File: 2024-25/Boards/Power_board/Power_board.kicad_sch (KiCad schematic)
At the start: 17 parts, among them J1 430451001

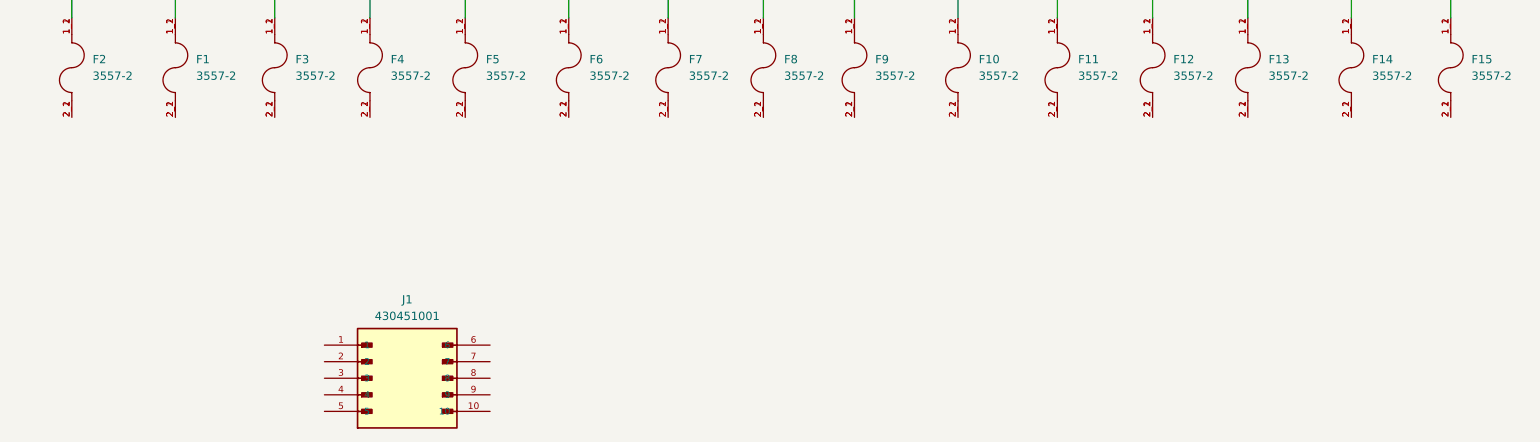
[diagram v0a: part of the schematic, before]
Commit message: added busbar board
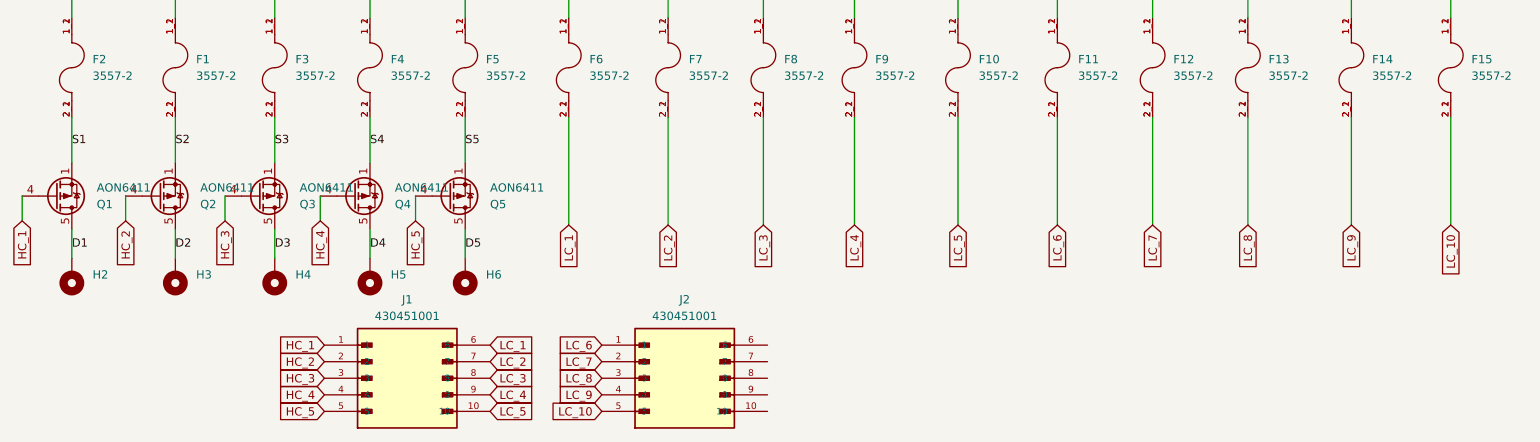
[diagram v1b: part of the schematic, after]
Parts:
- added H2, H3, H4, H5, H6: MountingHole_Pad, MountingHole:MountingHole_5.3mm_M5_Pad, symbol Mechanical:MountingHole_Pad
- added J2: 430451001, 0430451001:MOLEX_430451001, symbol 0430451001:430451001
- added Q1, Q2, Q3, Q4, Q5: AON6411, Package_DFN_QFN:AO_DFN-8-1EP_5.55x5.2mm_P1.27mm_EP4.12x4.6mm, symbol Transistor_FET:AON6411
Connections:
- net S4: now reaches F4.2_1, F4.2_2
- net S4: now also Q4.1 (S), Q4.2 (S), Q4.3 (S)
- net S5: now reaches F5.2_1, F5.2_2
- net S5: now also Q5.1 (S), Q5.2 (S), Q5.3 (S)
- net LC_3: now reaches F8.2_1, F8.2_2
- net LC_3: now also J1.8
- net S3: now reaches F3.2_1, F3.2_2
- net S3: now also Q3.1 (S), Q3.2 (S), Q3.3 (S)
- net LC_7: now reaches F12.2_1, F12.2_2
- net LC_7: now also J2.2
- net S1: now reaches F2.2_1, F2.2_2
- net S1: now also Q1.1 (S), Q1.2 (S), Q1.3 (S)
- net S2: now reaches F1.2_1, F1.2_2
- net S2: now also Q2.1 (S), Q2.2 (S), Q2.3 (S)
- net HC_1: now reaches J1.1
- net HC_1: now also Q1.4 (G)
- net LC_5: now reaches J1.10
- net LC_5: now also F10.2_1, F10.2_2
- net HC_2: now reaches J1.2
- net HC_2: now also Q2.4 (G)
- net HC_3: now reaches J1.3
- net HC_3: now also Q3.4 (G)
- net HC_4: now reaches J1.4
- net HC_4: now also Q4.4 (G)
- net HC_5: now reaches J1.5
- net HC_5: now also Q5.4 (G)
- net LC_1: now reaches J1.6
- net LC_1: now also F6.2_1, F6.2_2
- net LC_2: now reaches J1.7
- net LC_2: now also F7.2_1, F7.2_2
- net LC_4: now reaches J1.9
- net LC_4: now also F9.2_1, F9.2_2
- net LC_8: now reaches F13.2_1, F13.2_2
- net LC_8: now also J2.3
- net LC_9: now reaches F14.2_1, F14.2_2
- net LC_9: now also J2.4
- net LC_6: now reaches F11.2_1, F11.2_2
- net LC_6: now also J2.1
- net LC_10: now reaches F15.2_1, F15.2_2
- net LC_10: now also J2.5
- new net D1: H2.1, Q1.5 (D)
- new net D2: H3.1, Q2.5 (D)
- new net D3: H4.1, Q3.5 (D)
- new net D4: H5.1, Q4.5 (D)
- new net D5: H6.1, Q5.5 (D)

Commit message: organizational changes
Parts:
- added H7: MountingHole_Pad, MountingHole:MountingHole_5.3mm_M5_Pad, symbol Mechanical:MountingHole_Pad
- added Q10, Q6, Q7, Q8, Q9: AO3400, Package_TO_SOT_SMD:SOT-23-3, symbol Simulation_SPICE:NMOS
- added R1, R2, R3, R4, R5: 10k, symbol Device:R_Small_US
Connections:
- net HC_1: now also Q6.2 (G); no longer Q1.4 (G)
- net HC_2: now also Q7.2 (G); no longer Q2.4 (G)
- net HC_3: now also Q8.2 (G); no longer Q3.4 (G)
- net HC_4: now also Q9.2 (G); no longer Q4.4 (G)
- net HC_5: now also Q10.2 (G); no longer Q5.4 (G)
- net 12V+: now reaches F1.1_1, F1.1_2, F10.1_1, F10.1_2, F11.1_1, F11.1_2, F12.1_1, F12.1_2, F13.1_1, F13.1_2, F14.1_1, F14.1_2, F15.1_1, F15.1_2, F2.1_1, F2.1_2, F3.1_1, F3.1_2, F4.1_1, F4.1_2, F5.1_1, F5.1_2, F6.1_1, F6.1_2, F7.1_1, F7.1_2, F8.1_1, F8.1_2, F9.1_1, F9.1_2, H1.1
- net 12V+: now also R1.1, R2.1, R3.1, R4.1, R5.1
- net GND: now reaches J2.10
- net GND: now also J2.6, J2.7, J2.8, J2.9, H7.1, Q10.3 (S), Q6.3 (S), Q7.3 (S), Q8.3 (S), Q9.3 (S)
- new net: Q4.4 (G), Q9.1 (D), R4.2
- new net: Q1.4 (G), Q6.1 (D), R1.2
- new net: Q2.4 (G), Q7.1 (D), R2.2
- new net: Q10.1 (D), Q5.4 (G), R5.2
- new net: Q3.4 (G), Q8.1 (D), R3.2
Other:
- note added: "Battery negative terminal"
- note added: "Battery positive terminal"
- moved on the sheet: F1, F10, F11, F12, F13, F14, F15, F2, F3, F4, F5, F6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

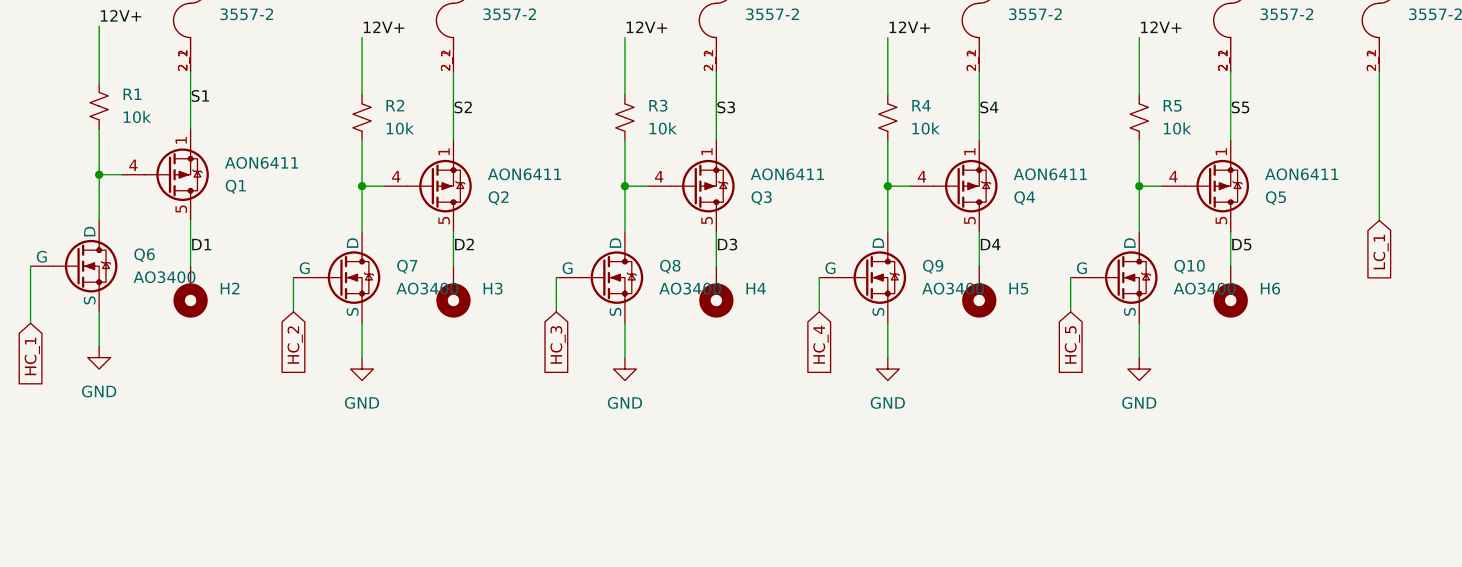
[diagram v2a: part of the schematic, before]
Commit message: accum and HV box schm
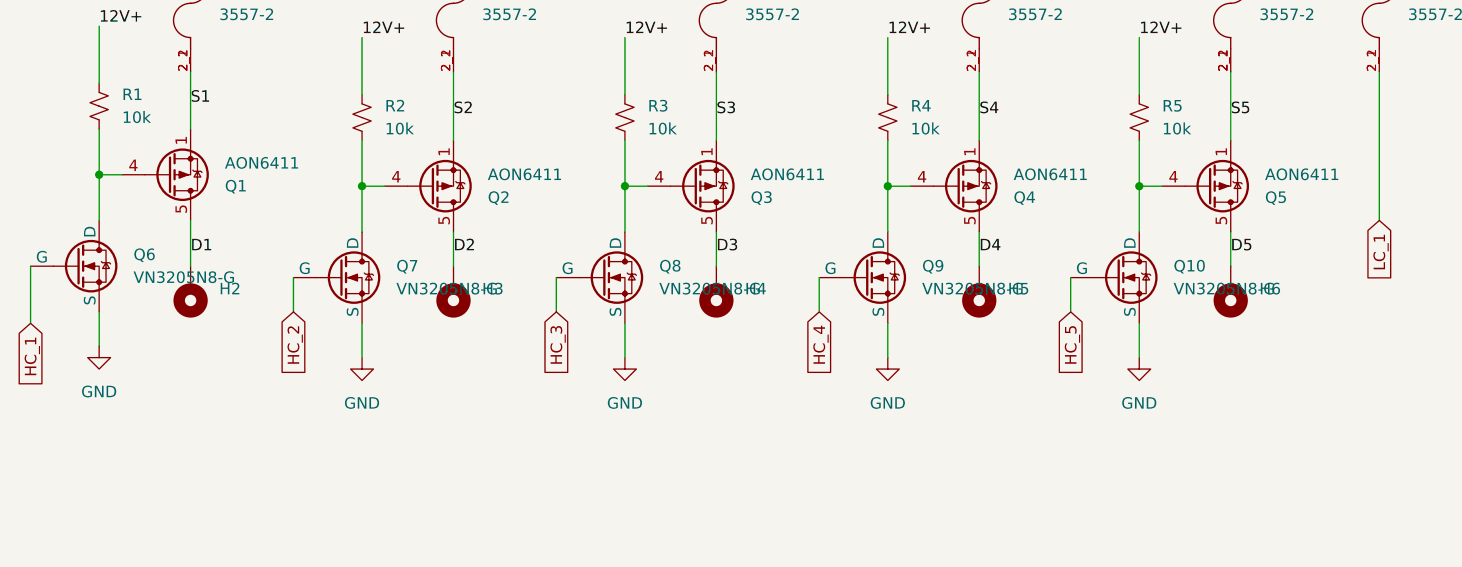
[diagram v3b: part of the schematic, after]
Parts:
- Q10, Q6, Q7, Q8, Q9: value AO3400 -> VN3205N8-G; footprint Package_TO_SOT_SMD:SOT-23-3 -> VN3205N8-G:AMP_PHA-1_
- R1, R2, R3, R4, R5: footprint (none) -> Resistor_SMD:R_0805_2012Metric_Pad1.20x1.40mm_HandSolder

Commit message: full schem
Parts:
- added J3: Conn_01x06_Socket, symbol Connector:Conn_01x06_Socket
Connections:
- net D1 is gone; now on net HC_1: H2.1, Q1.5 (D)
- net D2 is gone; now on net HC_2: H3.1, Q2.5 (D)
- net D3 is gone; now on net HC_3: H4.1, Q3.5 (D)
- net D4 is gone; now on net HC_4: H5.1, Q4.5 (D)
- net D5 is gone; now on net HC_5: H6.1, Q5.5 (D)
- net HC_1: no longer Q6.2 (G)
- net HC_2: no longer Q7.2 (G)
- net HC_3: no longer Q8.2 (G)
- net HC_4: no longer Q9.2 (G)
- net HC_5: no longer Q10.2 (G)
- new net HC_1_pwm: J3.1 (Pin_1), Q6.2 (G)
- new net HC_2_pwm: J3.2 (Pin_2), Q7.2 (G)
- new net HC_3_pwm: J3.3 (Pin_3), Q8.2 (G)
- new net HC_4_pwm: J3.4 (Pin_4), Q9.2 (G)
- new net HC_5_pwm: J3.5 (Pin_5), Q10.2 (G)

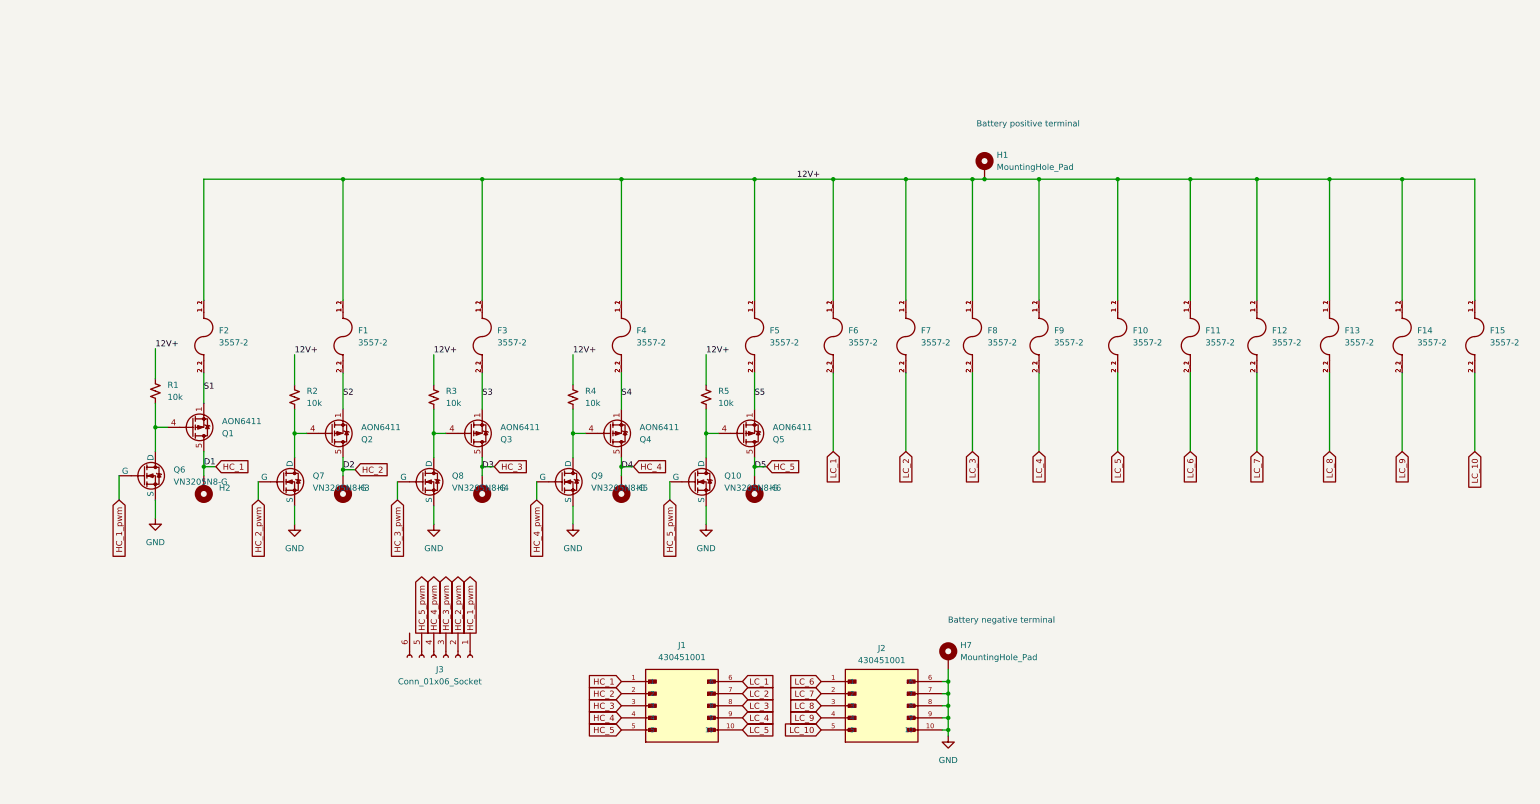
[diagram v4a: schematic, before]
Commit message: Removed extra fuses/high current switches/extra connectors
Removed said items, updated footprints, PCB, and symbols for power board
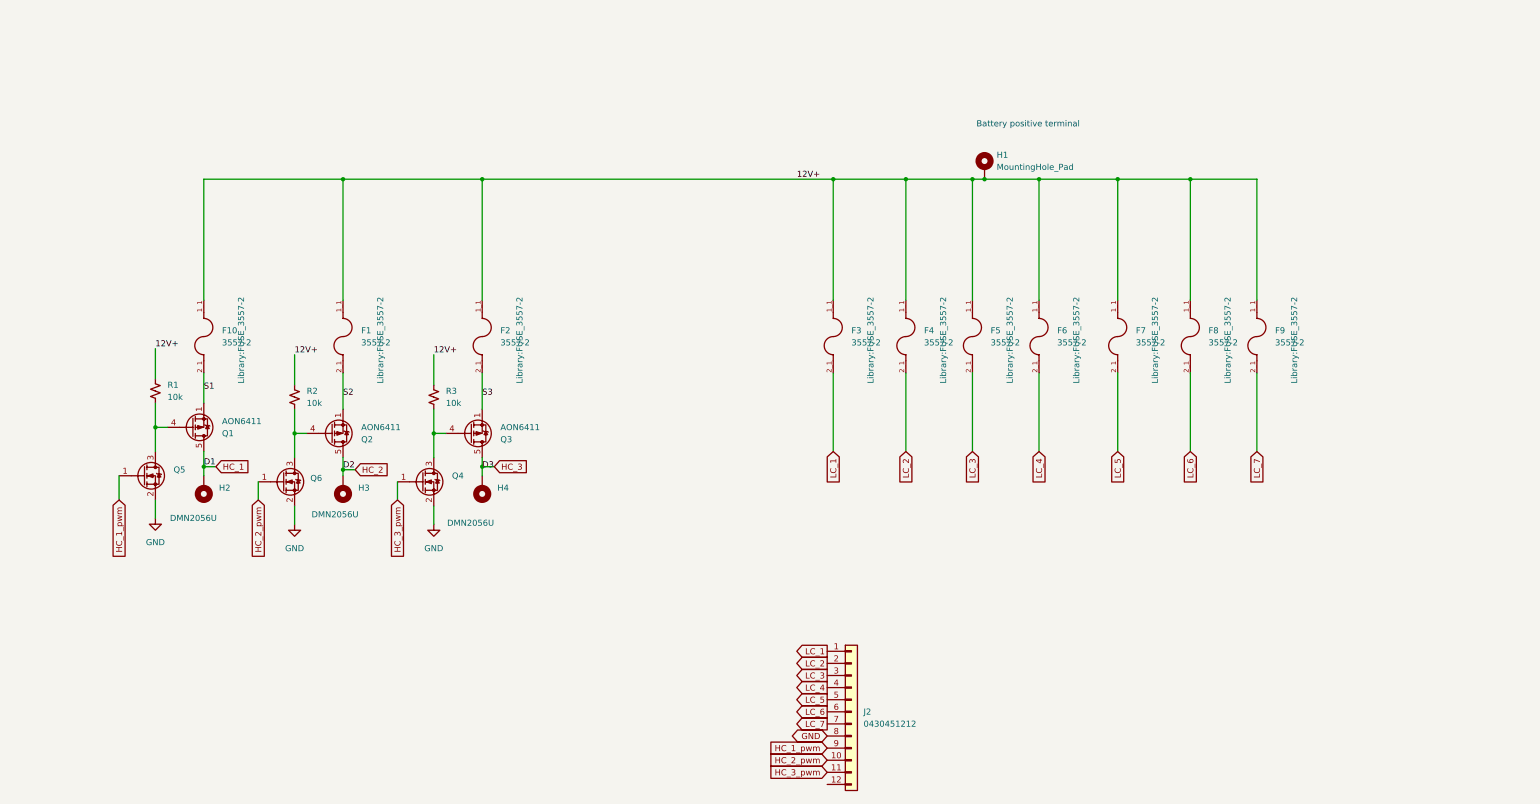
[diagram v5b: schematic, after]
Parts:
- removed F1, F10, F11, F12, F13, F14, F15, F2, F3, F4, F5, F6, F7, F8, F9: 3557-2, 3557-2:FUSE_3557-2, symbol 3557-2:3557-2
- removed H5, H6, H7: MountingHole_Pad, MountingHole:MountingHole_5.3mm_M5_Pad, symbol Mechanical:MountingHole_Pad
- removed J1, J2: 430451001, 0430451001:MOLEX_430451001, symbol 0430451001:430451001
- removed J3: Conn_01x06_Socket, symbol Connector:Conn_01x06_Socket
- removed Q10, Q6, Q7, Q8, Q9: VN3205N8-G, VN3205N8-G:AMP_PHA-1_, symbol Simulation_SPICE:NMOS
- removed Q4, Q5: AON6411, Package_DFN_QFN:AO_DFN-8-1EP_5.55x5.2mm_P1.27mm_EP4.12x4.6mm, symbol Transistor_FET:AON6411
- removed R4, R5: 10k, Resistor_SMD:R_0805_2012Metric_Pad1.20x1.40mm_HandSolder, symbol Device:R_Small_US
- added F1, F10, F2, F3, F4, F5, F6, F7, F8, F9: 3557-2, Library:FUSE_3557-2, symbol New_Library:3557-2
- added J2: 0430451212, Connector_Molex:Molex_Micro-Fit_3.0_43045-1212_2x06_P3.00mm_Vertical, symbol Connector_Generic:Conn_01x12
- added Q4, Q5, Q6: DMN2056U, Package_TO_SOT_SMD:SOT-23, symbol Transistor_FET:DMN2056U
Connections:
- net 12V+: now also F1.1_1, F10.1_1, F2.1_1, F3.1_1, F4.1_1, F5.1_1, F6.1_1, F7.1_1, F8.1_1, F9.1_1
- net GND: now also J2.8 (Pin_8), Q4.2 (S), Q5.2 (S), Q6.2 (S)
- net HC_1_pwm: now also J2.9 (Pin_9), Q5.1 (G)
- net HC_2_pwm: now also J2.10 (Pin_10), Q6.1 (G)
- net HC_3_pwm: now also J2.11 (Pin_11), Q4.1 (G)
- net LC_1: now also F3.2_1, J2.1 (Pin_1)
- net LC_2: now also F4.2_1, J2.2 (Pin_2)
- net LC_3: now also F5.2_1, J2.3 (Pin_3)
- net LC_4: now also F6.2_1, J2.4 (Pin_4)
- net LC_5: now also F7.2_1, J2.5 (Pin_5)
- net LC_6: now also F8.2_1, J2.6 (Pin_6)
- net LC_7: now also F9.2_1, J2.7 (Pin_7)
- net S1: now also F10.2_1
- net S2: now also F1.2_1
- net S3: now also F2.2_1
- net at Q1.4 (G), R1.2: now also Q5.3 (D)
- net at Q2.4 (G), R2.2: now also Q6.3 (D)
- net at Q3.4 (G), R3.2: now also Q4.3 (D)
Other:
- note removed: "Battery negative terminal"

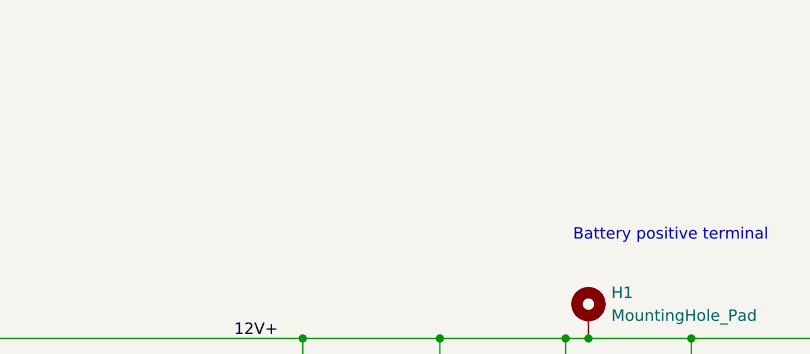
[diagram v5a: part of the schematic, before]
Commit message: laid out power board
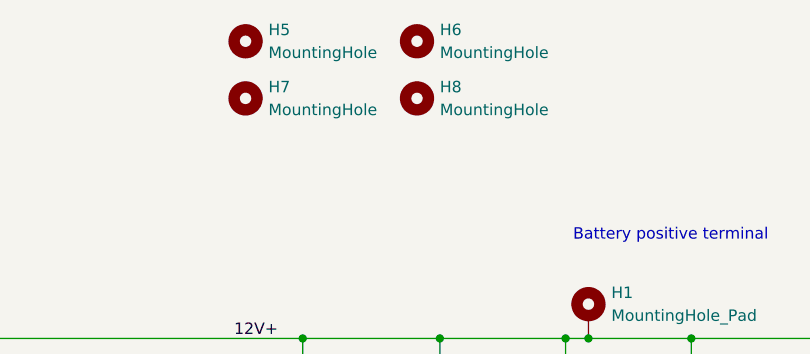
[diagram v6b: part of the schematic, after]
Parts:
- added H5, H6, H7, H8: MountingHole, MountingHole:MountingHole_5.3mm_M5, symbol Mechanical:MountingHole

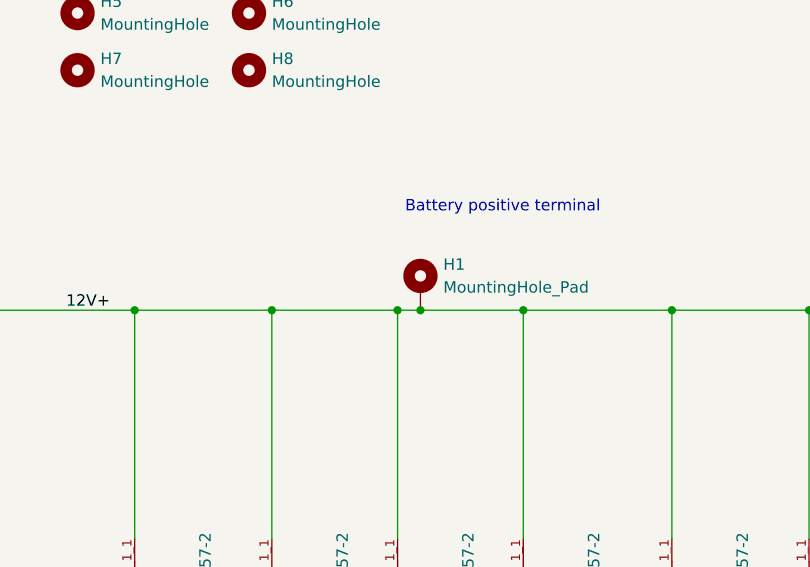
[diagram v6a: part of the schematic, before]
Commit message: added extra 12 V ring terminal for extra current input capability
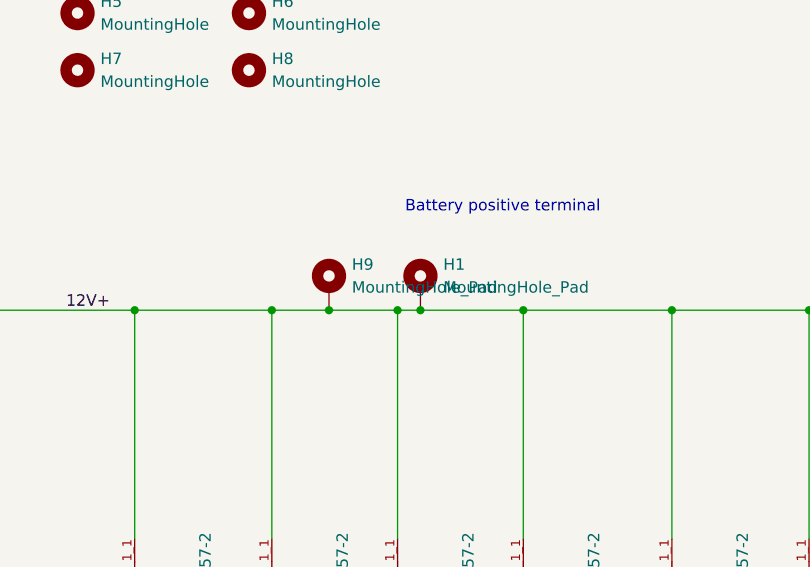
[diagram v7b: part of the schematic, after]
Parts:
- added H9: MountingHole_Pad, MountingHole:MountingHole_5.3mm_M5_Pad, symbol Mechanical:MountingHole_Pad
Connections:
- net 12V+: now also H9.1
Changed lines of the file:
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@@
 	)
 	(junction
+		(at 217.17 88.9)
+		(diameter 0)
+		(color 0 0 0 0)
+	)
+	(junction
 		(at 53.34 140.97)
 		(diameter 0)
@@
 	(wire
 		(pts
+			(xy 217.17 88.9) (xy 210.82 88.9)
+		)
+		(stroke
+			(width 0)
+			(type default)
+		)
+	)
+	(wire
+		(pts
 			(xy 63.5 149.225) (xy 66.04 149.225)
 		)
@@
 	(wire
 		(pts
-			(xy 224.79 88.9) (xy 210.82 88.9)
+			(xy 224.79 88.9) (xy 217.17 88.9)
 		)
 		(stroke
@@
 					(unit 1)
 				)
+			)
+		)
+	)
+	(symbol
+		(lib_id "Mechanical:MountingHole_Pad")
+		(at 217.17 86.36 0)
+		(unit 1)
+		(exclude_from_sim yes)
+		(in_bom no)
+		(on_board yes)
+		(dnp no)
+		(fields_autoplaced yes)
+		(property "Reference" "H9"
+			(at 219.71 83.8199 0)
+			(effects
+				(font
+					(size 1.27 1.27)
+				)
+				(justify left)
+			)
+		)
+		(property "Value" "MountingHole_Pad"
+			(at 219.71 86.3599 0)
+			(effects
+				(font
+					(size 1.27 1.27)
+				)
+				(justify left)
+			)
+		)
+		(property "Footprint" "MountingHole:MountingHole_5.3mm_M5_Pad"
+			(at 217.17 86.36 0)
+			(effects
+				(font
+					(size 1.27 1.27)
+				)
+				(hide yes)
+			)
+		)
+		(property "Datasheet" "~"
+			(at 217.17 86.36 0)
+			(effects
+				(font
+					(size 1.27 1.27)
+				)
+				(hide yes)
+			)
+		)
+		(property "Description" "Mounting Hole with connection"
+			(at 217.17 86.36 0)
+			(effects
+				(font
+					(size 1.27 1.27)
+				)
+				(hide yes)
+			)
+		)
+		(pin "1"
+		)
+		(instances
+			(project "Power_board"
+				(path "/c7bceacb-49ea-4a13-95e2-5e56f8e6630a"
+					(reference "H9")
+					(unit 1)
+				)
